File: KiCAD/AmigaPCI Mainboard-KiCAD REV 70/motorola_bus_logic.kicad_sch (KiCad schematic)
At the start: 30 parts, among them U231 74LVC08, U802 74LVC245, U803 74LVC245, U804 74LVC245, U805 74LVC245, U806 74LVC245, U807 74LVC245, U808 74LVC245, U809 74LVC245, U810 74LVC16646, U820 74LVC245, U821 74LVC245, U822 74LVC245, U823 74LVC245

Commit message: Add JLCPCB part numbers and fix 74LVC244 footprints.
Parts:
- C802, C803, C804, C805, C806, C807, C808, C809, C810, C811, C812, C813, C814, C815, C824, C825: LCSC (none) -> C14663
- U231: LCSC (none) -> C6053
- U802, U803, U804, U805, U806, U807, U808, U809, U820, U821, U822, U823: LCSC (none) -> C7848
- U810: LCSC (none) -> C2869631

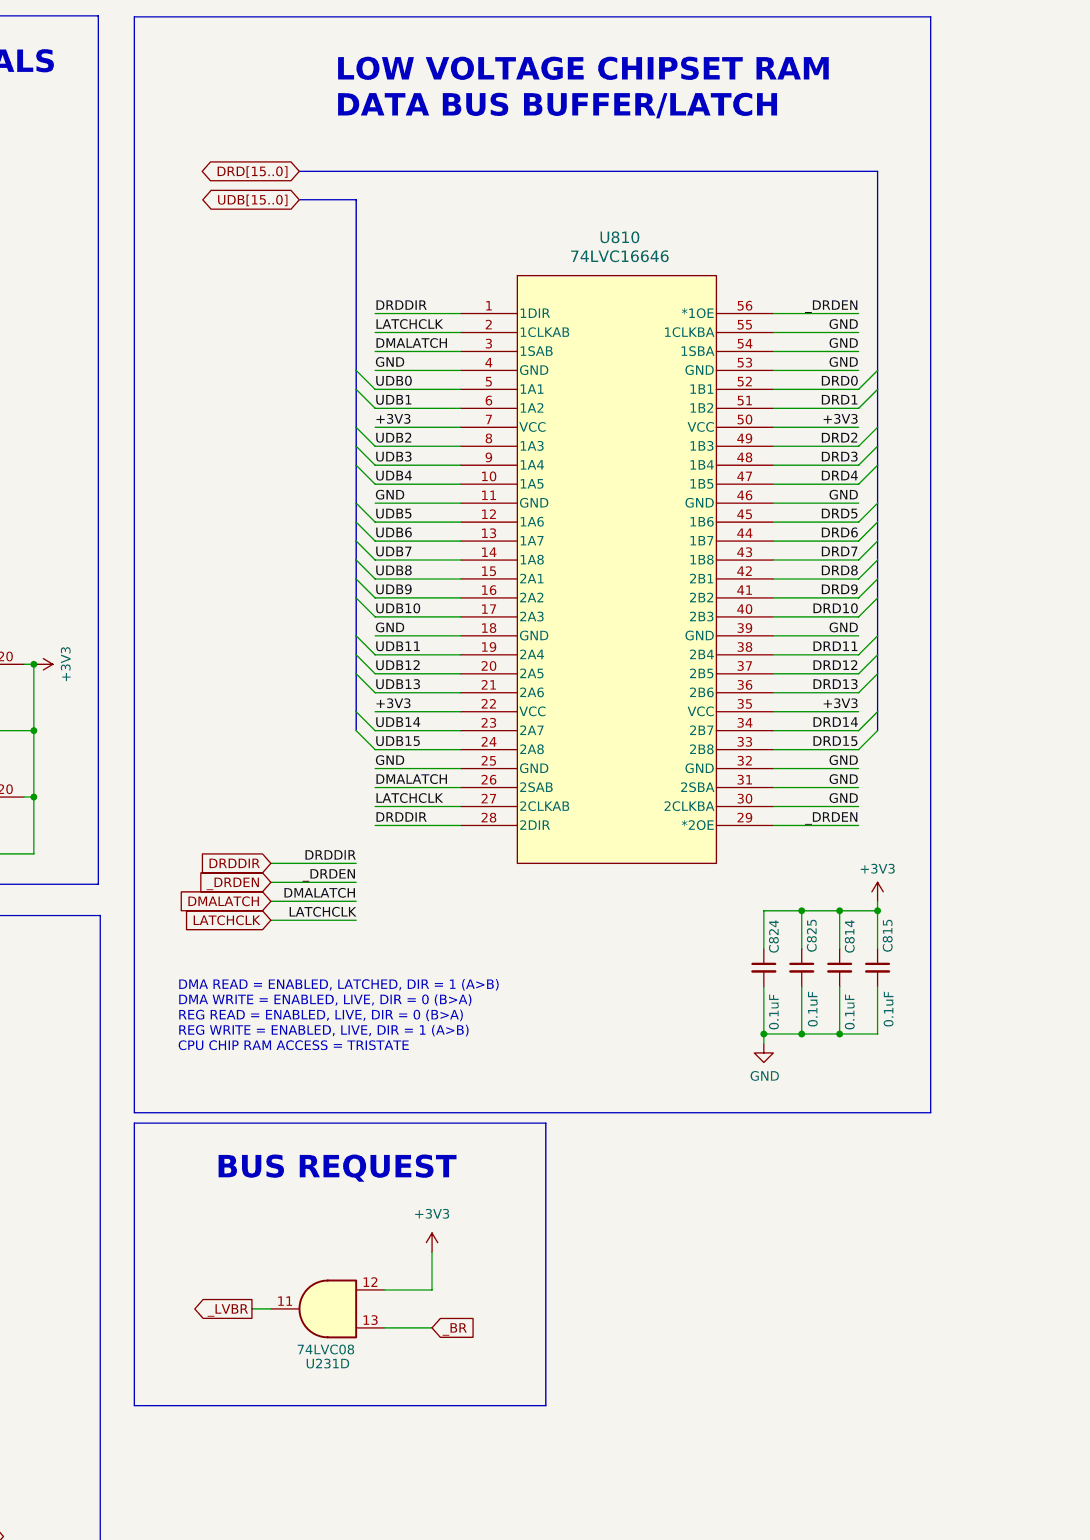
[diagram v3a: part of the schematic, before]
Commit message: Updates to revision 7 board.
Change U810 to 74LVC245 buffers
Add CDAC to U712
Add address latch to CIAs
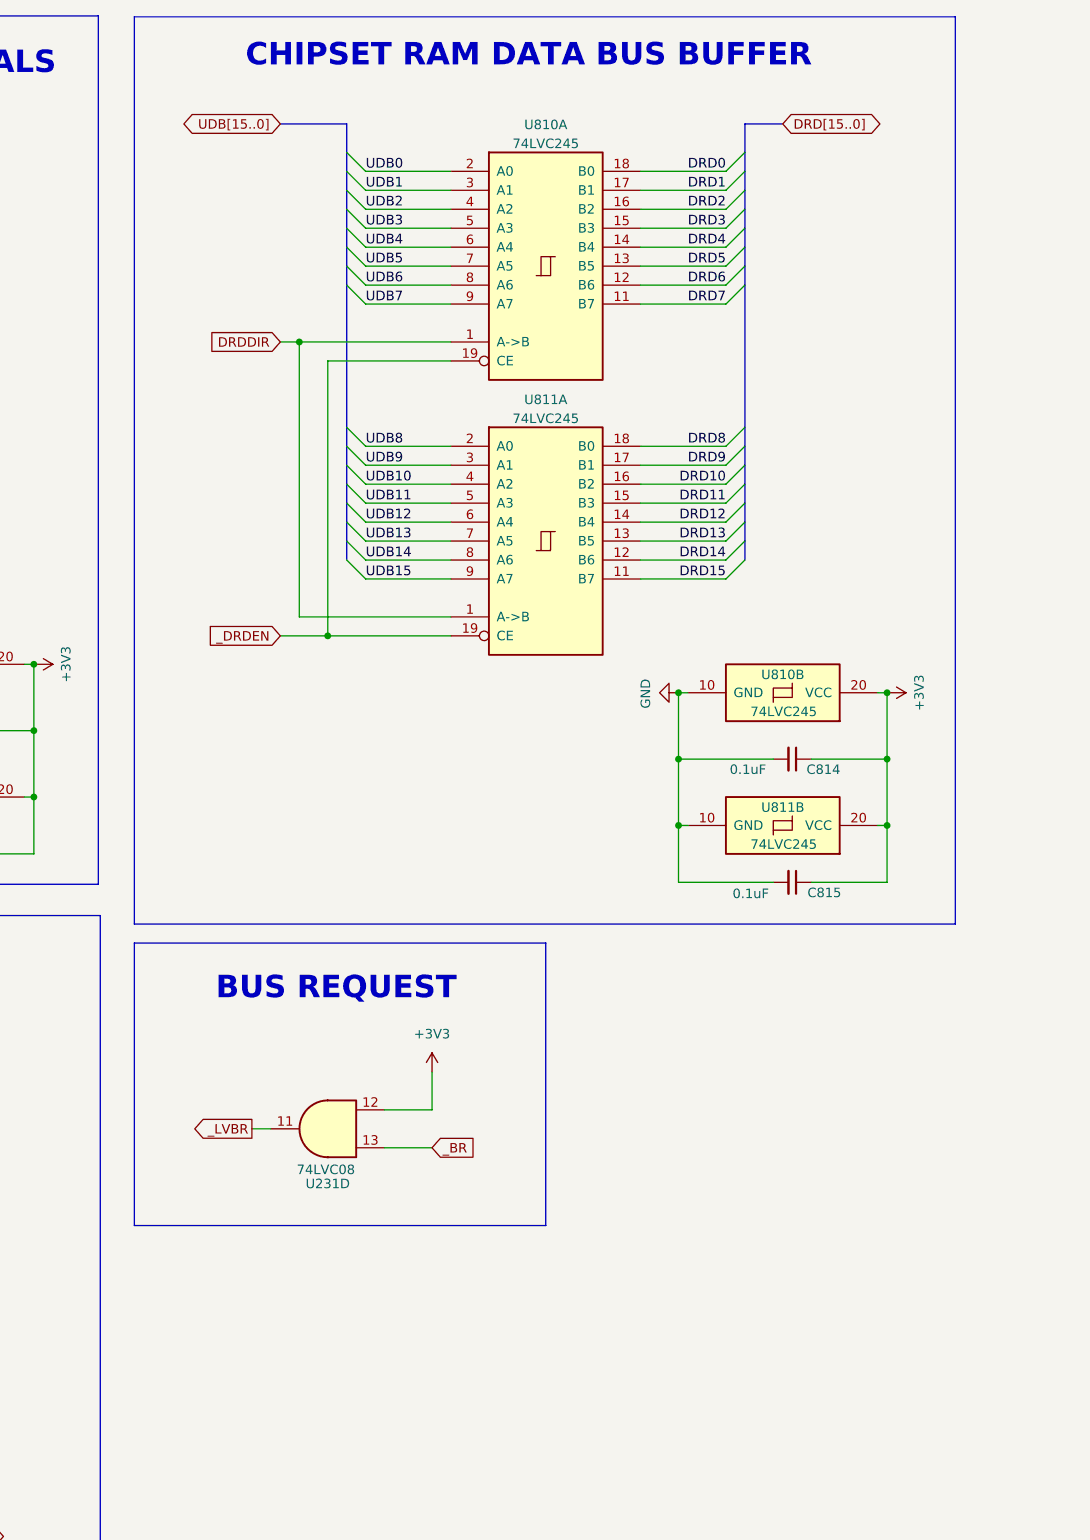
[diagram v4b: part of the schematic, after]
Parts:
- removed C824, C825: 0.1uF, Capacitor_SMD:C_0603_1608Metric, symbol Device:C_Small
- removed U810: 74LVC16646, Package_SO:SSOP-56_7.5x18.5mm_P0.635mm, symbol AmigaPCI-Symbols:74LVC16646
- added U810, U811: 74LVC245, Package_SO:TSSOP-20_4.4x6.5mm_P0.65mm, symbol AmigaPCI-Symbols:74LVC245
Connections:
- net +3V3: now also U810.20 (VCC), U811.20 (VCC)
- net DRD0: now also U810.18 (B0)
- net DRD1: now also U810.17 (B1)
- net DRD10: now also U811.16 (B2)
- net DRD11: now also U811.15 (B3)
- net DRD12: now also U811.14 (B4)
- net DRD13: now also U811.13 (B5)
- net DRD14: now also U811.12 (B6)
- net DRD15: now also U811.11 (B7)
- net DRD2: now also U810.16 (B2)
- net DRD3: now also U810.15 (B3)
- net DRD4: now also U810.14 (B4)
- net DRD5: now also U810.13 (B5)
- net DRD6: now also U810.12 (B6)
- net DRD7: now also U810.11 (B7)
- net DRD8: now also U811.18 (B0)
- net DRD9: now also U811.17 (B1)
- net DRDDIR: now also U810.1 (A->B), U811.1 (A->B)
- net GND: now also U810.10 (GND), U811.10 (GND)
- net UDB0: now also U810.2 (A0)
- net UDB1: now also U810.3 (A1)
- net UDB10: now also U811.4 (A2)
- net UDB11: now also U811.5 (A3)
- net UDB12: now also U811.6 (A4)
- net UDB13: now also U811.7 (A5)
- net UDB14: now also U811.8 (A6)
- net UDB15: now also U811.9 (A7)
- net UDB2: now also U810.4 (A2)
- net UDB3: now also U810.5 (A3)
- net UDB4: now also U810.6 (A4)
- net UDB5: now also U810.7 (A5)
- net UDB6: now also U810.8 (A6)
- net UDB7: now also U810.9 (A7)
- net UDB8: now also U811.2 (A0)
- net UDB9: now also U811.3 (A1)
- net _DRDEN: now also U810.19 (CE), U811.19 (CE)
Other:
- note added: "CHIPSET RAM DATA BUS BUFFER"
- note removed: "DMA READ = ENABLED, LATCHED, DIR = 1 (A>B) DMA WRITE = ENABLED, LIVE, DIR = 0 (B>A) REG READ = ENABLED, LIVE, DIR = 0 (B>A) REG WRITE = ENABLED, LIVE, DIR = 1 (A>B) CPU CHIP RAM ACCESS = TRISTATE"
- note removed: "LOW VOLTAGE CHIPSET RAM DATA BUS BUFFER/LATCH"
- moved on the sheet: U231D
